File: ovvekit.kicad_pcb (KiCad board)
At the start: 4 copper layers, 75 x 76 mm, 139 parts, among them IC1 MAX4466EXK+T, J1 ESP_PROG_JTAG, J2 ESP_PROG_UART, J201 Power_Planes, Q201 SI4435DY_GSD, SW1 SW_Push, SW2 SW_Push, SW3 SW_Push, SW4 SW_Push, U1 ESP32-WROOM-32, U201 AP2112K-3.3, U203 AMS1117-3.3

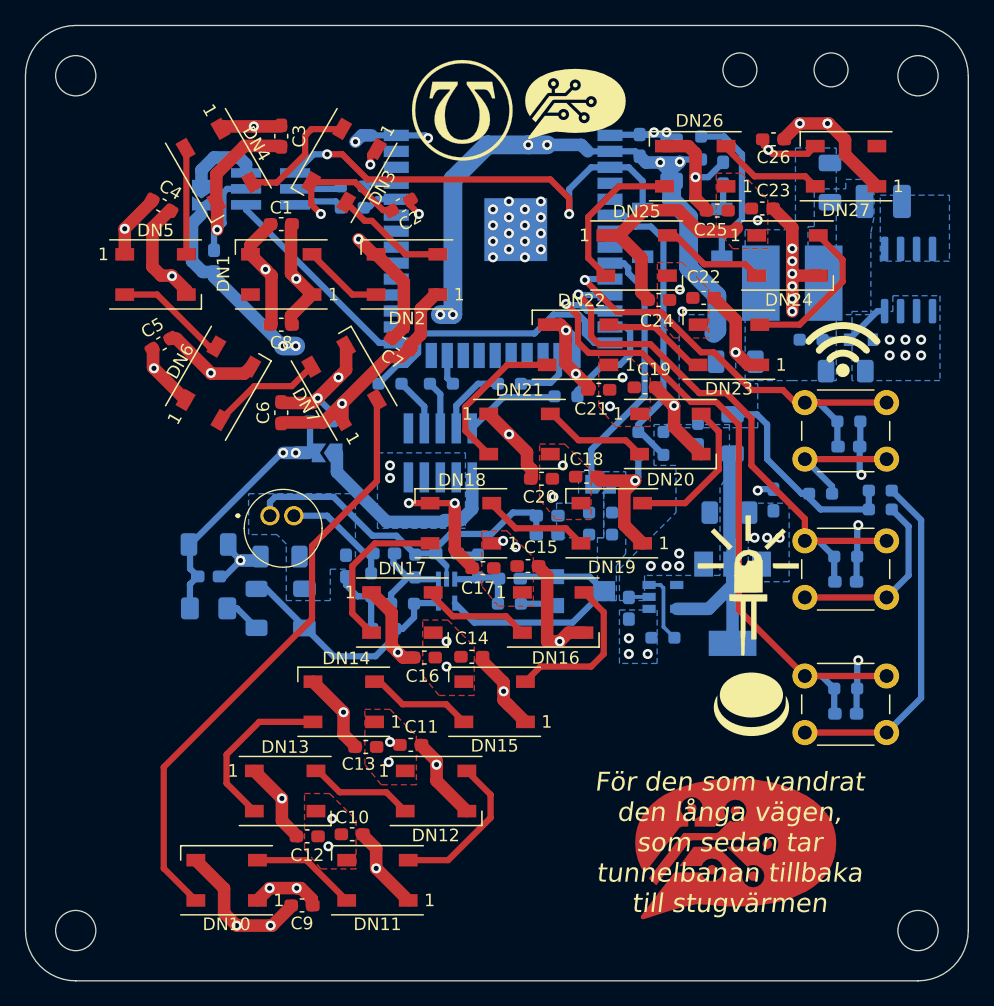
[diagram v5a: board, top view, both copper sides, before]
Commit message: Update to correct OP-amp. This is the version sent to production.
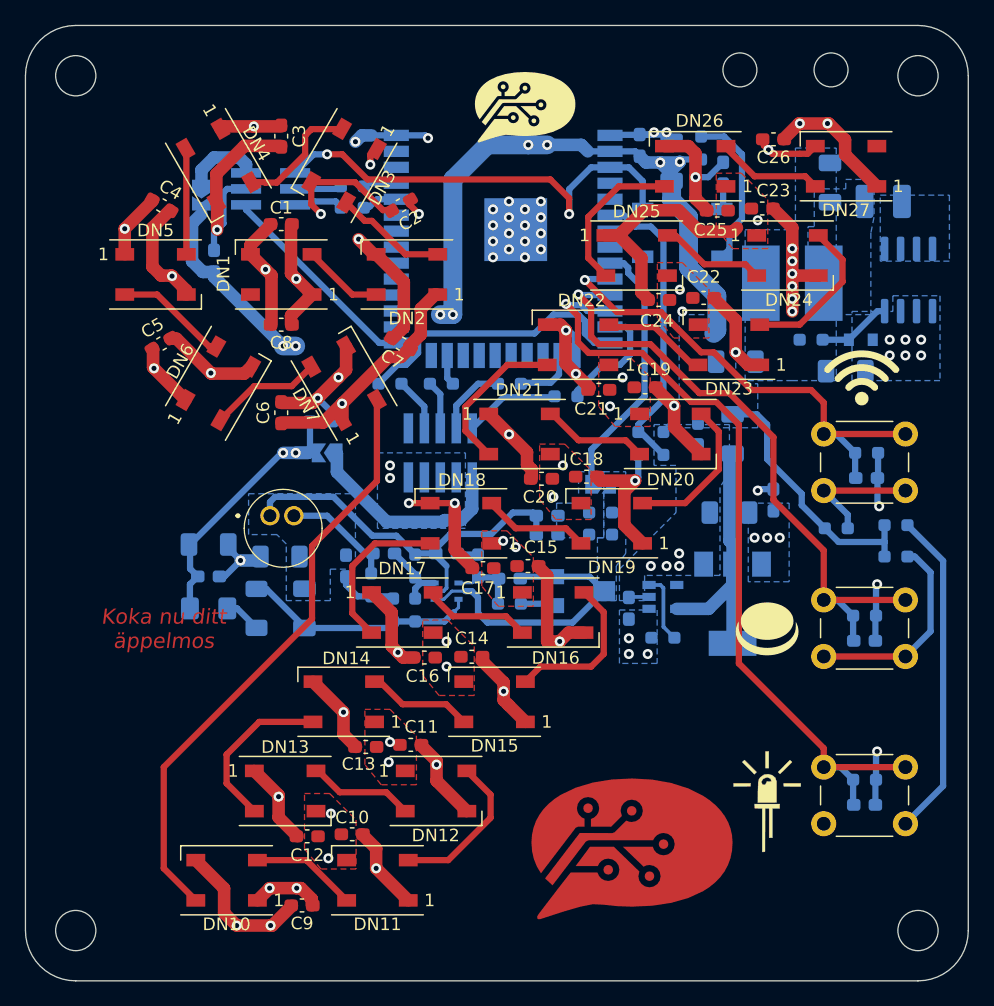
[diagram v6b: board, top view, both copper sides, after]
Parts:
- removed IC1: MAX4466EXK+T, Special_Parts:SOT65P210X110-5N
- removed the svg2mod at (8.75, -0.25)
- added U2: MCP6001x-LT, Package_TO_SOT_SMD:SOT-353_SC-70-5, B.Cu at (7.50, 38.0)
- button_5mm_SilkScreen: footprint SymbolsOST:button_6mm_SilkScreen -> SymbolsOST:button_5mm_SilkScreen
- led_12mm_SilkScreen: footprint SymbolsOST:led_12mm_SilkScreen -> SymbolsOST:led_8mm_SilkScreen
- svg2mod: footprint SymbolsOST:admittansen_16mm_SilkScreen -> SymbolsOST:admittansen_8mm_SilkScreen
- moved svg2mod 33.2 mm to (28.0, 52.8)
- moved svg2mod 23.7 mm to (-6.50, 54.0)
- moved led_12mm_SilkScreen 16.8 mm to (33.0, 54.8)
- moved REF** 11.7 mm to (17.5, 52.5)
- moved svg2mod 8.25 mm to (22.2, 58.5)
- moved C102 7.40 mm to (40.8, 55.0)
- moved R106 7.40 mm to (40.8, 53.0)
- moved SW3 7.40 mm to (37.5, 52.0)
- moved REF** 6.56 mm to (21.2, 61.5)
- moved button_5mm_SilkScreen 6.13 mm to (33.0, 41.0)
- moved C101 4.93 mm to (40.8, 42.0)
- moved R104 4.93 mm to (40.8, 40.0)
- moved SW2 4.93 mm to (37.5, 38.7)
- moved svg2mod 4.01 mm to (13.8, -0.50)
- moved R103 3.95 mm to (43.2, 35.2)
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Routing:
- net BTN_3: track 56.1 -> 64.0 mm
- net BTN_2: track 44.6 -> 50.1 mm
- net BTN_1: track 35.3 -> 39.3 mm
- net +3V3: track 106.1 -> 109.8 mm
- net Net-(C30-Pad1): track 20.8 -> 23.8 mm
- net /sound/AUDIO_AMP+: track 7.51 -> 5.74 mm
- net GNDA: track 30.0 -> 31.7 mm
- net Net-(R105-Pad2): track 27.9 -> 26.2 mm
- net Net-(R103-Pad2): track 14.8 -> 16.4 mm
- net Net-(C27-Pad1): track 5.73 -> 4.93 mm
- net +3.3VA: track 19.4 -> 18.6 mm
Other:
- board text added: "Koka nu ditt äppelmos"

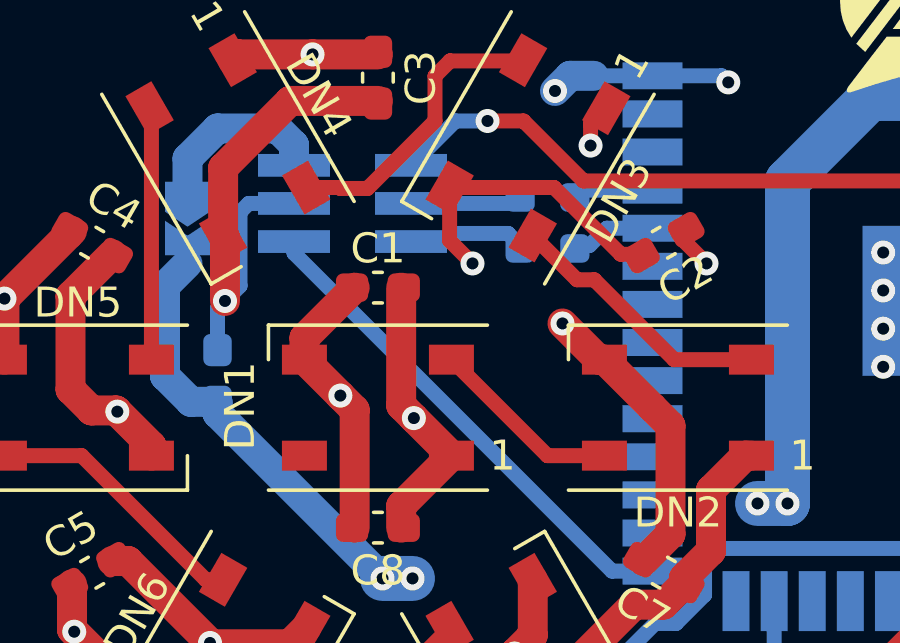
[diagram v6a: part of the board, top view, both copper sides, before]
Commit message: ... Forgot to connect the data line to esp32... It's done now.
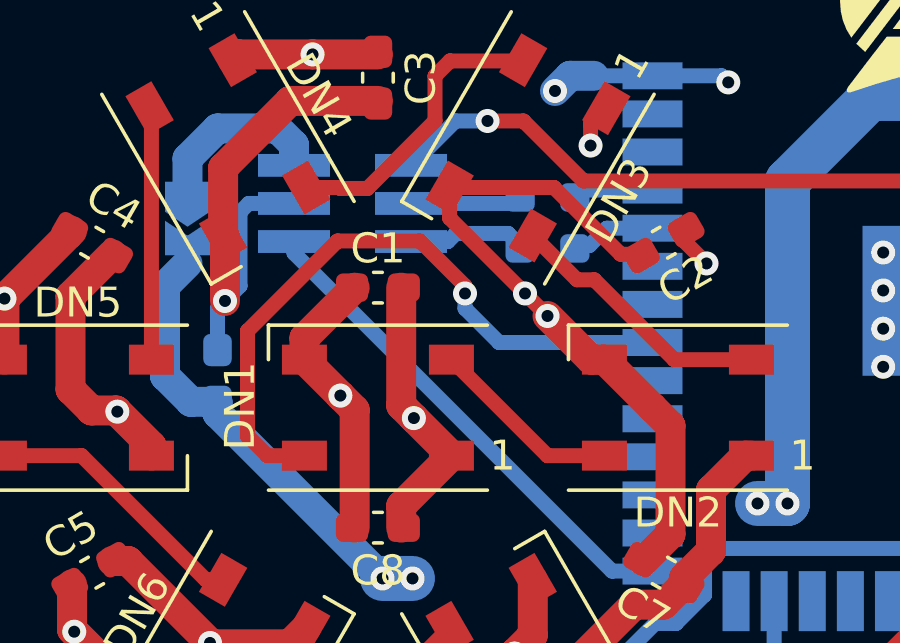
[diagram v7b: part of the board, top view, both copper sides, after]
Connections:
- DN1 pad 4: unconnected-(DN1-Pad4) -> WS2812B-DATA
- U1 pad 31: unconnected-(U1-Pad31) -> WS2812B-DATA
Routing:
- net WS2812B-DATA: track 0.00 -> 22.3 mm, vias 0 -> 1
- net GND: track 200.4 -> 203.8 mm

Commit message: Fixed version commited to JLC.
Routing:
- net Net-(R105-Pad2): track 26.2 -> 32.7 mm
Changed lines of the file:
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@@
   (layers
     (0 "F.Cu" signal)
-    (1 "In1.Cu" power)
-    (2 "In2.Cu" power)
+    (1 "In1.Cu" power "In_VCC.Cu")
+    (2 "In2.Cu" power "In_GND.Cu")
     (31 "B.Cu" signal)
     (32 "B.Adhes" user "B.Adhesive")
@@
   )
   (setup
+    (stackup
+      (layer "F.SilkS" (type "Top Silk Screen"))
+      (layer "F.Paste" (type "Top Solder Paste"))
+      (layer "F.Mask" (type "Top Solder Mask") (thickness 0.01))
+      (layer "F.Cu" (type "copper") (thickness 0.035))
+      (layer "dielectric 1" (type "core") (thickness 0.48) (material "FR4") (epsilon_r 4.5) (loss_tangent 0.02))
+      (layer "In1.Cu" (type "copper") (thickness 0.035))
+      (layer "dielectric 2" (type "prepreg") (thickness 0.48) (material "FR4") (epsilon_r 4.5) (loss_tangent 0.02))
+      (layer "In2.Cu" (type "copper") (thickness 0.035))
+      (layer "dielectric 3" (type "core") (thickness 0.48) (material "FR4") (epsilon_r 4.5) (loss_tangent 0.02))
+      (layer "B.Cu" (type "copper") (thickness 0.035))
+      (layer "B.Mask" (type "Bottom Solder Mask") (thickness 0.01))
+      (layer "B.Paste" (type "Bottom Solder Paste"))
+      (layer "B.SilkS" (type "Bottom Silk Screen"))
+      (copper_finish "None")
+      (dielectric_constraints no)
+    )
     (pad_to_mask_clearance 0)
     (grid_origin 40 54.25)
@@
   (segment (start 2.73 40.9325) (end 3.25 40.4125) (width 0.5) (layer "B.Cu") (net 49))
   (segment (start 5 40.4125) (end 7.3375 40.4125) (width 0.5) (layer "B.Cu") (net 49))
+  (segment (start 44 56.5) (end 37.5 56.5) (width 0.5) (layer "F.Cu") (net 52))
   (segment (start 47 53.5) (end 44 56.5) (width 0.5) (layer "B.Cu") (net 52))
   (segment (start 44.1625 32.75) (end 47 35.5875) (width 0.5) (layer "B.Cu") (net 52))
